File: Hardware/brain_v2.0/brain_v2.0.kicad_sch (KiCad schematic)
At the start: 84 parts, among them J1 Conn_01x02, J10 RFID, J11 Conn_01x05, J12 Conn_01x02, J13 Conn_01x02, J14 Conn_01x02, J15 Conn_01x04, J16 Conn_01x04, J2 Conn_01x02, J3 Conn_01x03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

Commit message: second version of brain
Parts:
- added TP7: TestPoint, TestPoint:TestPoint_Keystone_5010-5014_Multipurpose, symbol Connector:TestPoint
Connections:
- net GPIO0: now also TP7.1

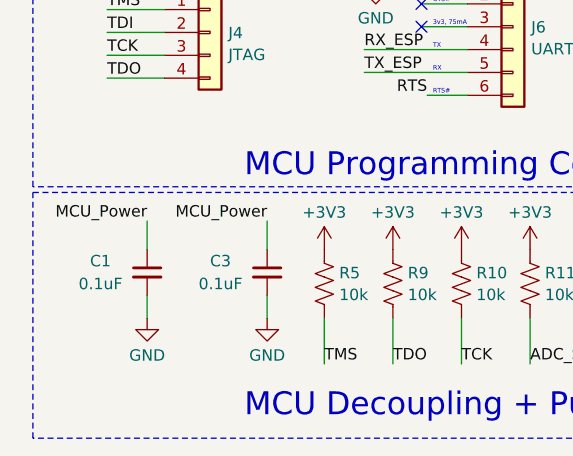
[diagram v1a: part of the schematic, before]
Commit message: creating PDS board and update other boards
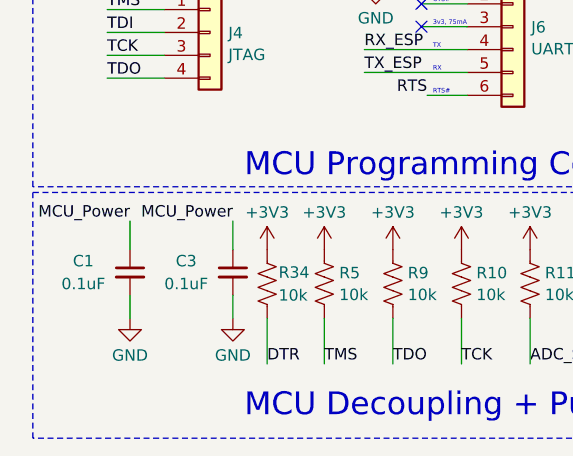
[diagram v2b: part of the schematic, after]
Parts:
- added R34: 10k, Resistor_SMD:R_1206_3216Metric, symbol Device:R_US
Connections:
- net +3V3: now also R34.1
- net DTR: now also R34.2
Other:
- moved on the sheet: C1, C3
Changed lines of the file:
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@@
     (stroke (width 0) (type default))
   )
-  (wire (pts (xy 24.765 190.5) (xy 24.765 187.96))
+  (wire (pts (xy 22.86 190.5) (xy 22.86 187.96))
     (stroke (width 0) (type default))
   )
@@
     (stroke (width 0) (type default))
   )
-  (wire (pts (xy 38.1 190.5) (xy 38.1 187.96))
+  (wire (pts (xy 34.29 190.5) (xy 34.29 187.96))
     (stroke (width 0) (type default))
   )
@@
     (stroke (width 0) (type default))
   )
-  (wire (pts (xy 38.1 179.705) (xy 38.1 182.88))
+  (wire (pts (xy 34.29 179.705) (xy 34.29 182.88))
     (stroke (width 0) (type default))
   )
@@
     (stroke (width 0) (type default))
   )
+  (wire (pts (xy 38.1 190.5) (xy 38.1 195.58))
+    (stroke (width 0) (type default))
+  )
   (wire (pts (xy 175.26 133.35) (xy 177.8 133.35))
     (stroke (width 0) (type default))
@@
     (stroke (width 0) (type default))
   )
-  (wire (pts (xy 24.765 179.705) (xy 24.765 182.88))
+  (wire (pts (xy 22.86 179.705) (xy 22.86 182.88))
     (stroke (width 0) (type default))
   )
@@
     (effects (font (size 1.27 1.27)) (justify left bottom))
   )
-  (label "MCU_Power" (at 38.1 179.705 180) (fields_autoplaced)
+  (label "MCU_Power" (at 34.29 179.705 180) (fields_autoplaced)
     (effects (font (size 1.27 1.27)) (justify right bottom))
   )
@@
     (effects (font (size 1.27 1.27)) (justify left bottom))
   )
+  (label "DTR" (at 38.1 195.58 0) (fields_autoplaced)
+    (effects (font (size 1.27 1.27)) (justify left bottom))
+  )
   (label "ADC_SDA" (at 246.38 148.59 0) (fields_autoplaced)
     (effects (font (size 1.27 1.27)) (justify left bottom))
@@
     (effects (font (size 1.27 1.27)) (justify left bottom))
   )
-  (label "MCU_Power" (at 24.765 179.705 180) (fields_autoplaced)
+  (label "MCU_Power" (at 22.86 179.705 180) (fields_autoplaced)
     (effects (font (size 1.27 1.27)) (justify right bottom))
   )
@@
     )
   )
-  (symbol (lib_id "device:C_Small") (at 24.765 185.42 0) (unit 1)
+  (symbol (lib_id "device:C_Small") (at 22.86 185.42 0) (unit 1)
     (in_bom yes) (on_board yes) (dnp no)
-    (property "Reference" "C1" (at 18.415 184.15 0)
+    (property "Reference" "C1" (at 16.51 184.15 0)
       (effects (font (size 1.27 1.27)) (justify left))
     )
-    (property "Value" "0.1uF" (at 17.145 186.69 0)
+    (property "Value" "0.1uF" (at 15.24 186.69 0)
       (effects (font (size 1.27 1.27)) (justify left))
     )
-    (property "Footprint" "Capacitor_SMD:C_0603_1608Metric" (at 24.765 185.42 0)
+    (property "Footprint" "Capacitor_SMD:C_0603_1608Metric" (at 22.86 185.42 0)
       (effects (font (size 1.27 1.27)) hide)
     )
-    (property "Datasheet" "~" (at 24.765 185.42 0)
+    (property "Datasheet" "~" (at 22.86 185.42 0)
       (effects (font (size 1.27 1.27)) hide)
     )
-    (property "Link" "https://www.digikey.com/en/products/detail/kemet/C0603C103F3GECAUTO/6826352" (at 24.765 185.42 0)
+    (property "Link" "https://www.digikey.com/en/products/detail/kemet/C0603C103F3GECAUTO/6826352" (at 22.86 185.42 0)
       (effects (font (size 1.27 1.27)) hide)
     )
-    (property "MPN" "C0603C103F3GECAUTO" (at 24.765 185.42 0)
+    (property "MPN" "C0603C103F3GECAUTO" (at 22.86 185.42 0)
       (effects (font (size 1.27 1.27)) hide)
     )
@@
     )
   )
-  (symbol (lib_id "power:GND") (at 24.765 190.5 0) (unit 1)
+  (symbol (lib_id "power:GND") (at 22.86 190.5 0) (unit 1)
     (in_bom yes) (on_board yes) (dnp no) (fields_autoplaced)
-    (property "Reference" "#PWR03" (at 24.765 196.85 0)
+    (property "Reference" "#PWR03" (at 22.86 196.85 0)
       (effects (font (size 1.27 1.27)) hide)
     )
-    (property "Value" "GND" (at 24.765 194.6331 0)
+    (property "Value" "GND" (at 22.86 194.6331 0)
       (effects (font (size 1.27 1.27)))
     )
-    (property "Footprint" "" (at 24.765 190.5 0)
+    (property "Footprint" "" (at 22.86 190.5 0)
       (effects (font (size 1.27 1.27)) hide)
     )
-    (property "Datasheet" "" (at 24.765 190.5 0)
+    (property "Datasheet" "" (at 22.86 190.5 0)
       (effects (font (size 1.27 1.27)) hide)
     )
@@
     )
   )
+  (symbol (lib_id "power:+3V3") (at 38.1 182.88 0) (unit 1)
+    (in_bom yes) (on_board yes) (dnp no) (fields_autoplaced)
+    (property "Reference" "#PWR059" (at 38.1 186.69 0)
+      (effects (font (size 1.27 1.27)) hide)
+    )
+    (property "Value" "+3V3" (at 38.1 178.7469 0)
+      (effects (font (size 1.27 1.27)))
+    )
+    (property "Footprint" "" (at 38.1 182.88 0)
+      (effects (font (size 1.27 1.27)) hide)
+    )
+    (property "Datasheet" "" (at 38.1 182.88 0)
+      (effects (font (size 1.27 1.27)) hide)
+    )
+    (pin "1")
+    (instances
+      (project "brain_v2.0"
+        (path "/1e1b062d-fad0-427c-a622-c5b8a80b5268"
+          (reference "#PWR059") (unit 1)
+        )
+      )
+    )
+  )
   (symbol (lib_id "Mechanical:MountingHole") (at 17.145 15.875 0) (unit 1)
     (in_bom yes) (on_board yes) (dnp no) (fields_autoplaced)
@@
     )
   )
-  (symbol (lib_id "power:GND") (at 38.1 190.5 0) (unit 1)
+  (symbol (lib_id "power:GND") (at 34.29 190.5 0) (unit 1)
     (in_bom yes) (on_board yes) (dnp no) (fields_autoplaced)
-    (property "Reference" "#PWR010" (at 38.1 196.85 0)
+    (property "Reference" "#PWR010" (at 34.29 196.85 0)
       (effects (font (size 1.27 1.27)) hide)
     )
-    (property "Value" "GND" (at 38.1 194.6331 0)
+    (property "Value" "GND" (at 34.29 194.6331 0)
       (effects (font (size 1.27 1.27)))
     )
-    (property "Footprint" "" (at 38.1 190.5 0)
+    (property "Footprint" "" (at 34.29 190.5 0)
       (effects (font (size 1.27 1.27)) hide)
     )
-    (property "Datasheet" "" (at 38.1 190.5 0)
+    (property "Datasheet" "" (at 34.29 190.5 0)
       (effects (font (size 1.27 1.27)) hide)
     )
@@
     )
   )
+  (symbol (lib_id "Device:R_US") (at 38.1 186.69 0) (unit 1)
+    (in_bom yes) (on_board yes) (dnp no)
+    (property "Reference" "R34" (at 39.37 185.42 0)
+      (effects (font (size 1.27 1.27)) (justify left))
+    )
+    (property "Value" "10k" (at 39.37 187.96 0)
+      (effects (font (size 1.27 1.27)) (justify left))
+    )
+    (property "Footprint" "Resistor_SMD:R_1206_3216Metric" (at 39.116 186.944 90)
+      (effects (font (size 1.27 1.27)) hide)
+    )
+    (property "Datasheet" "~" (at 38.1 186.69 0)
+      (effects (font (size 1.27 1.27)) hide)
+    )
+    (property "Link" "https://www.digikey.com/en/products/detail/susumu/HRG3216P-1002-B-T1/5762469" (at 38.1 186.69 0)
+      (effects (font (size 1.27 1.27)) hide)
+    )
+    (property "MPN" "HRG3216P-1002-B-T1" (at 38.1 186.69 0)
+      (effects (font (size 1.27 1.27)) hide)
+    )
+    (pin "1")
+    (pin "2")
+    (instances
+      (project "brain_v2.0"
+        (path "/1e1b062d-fad0-427c-a622-c5b8a80b5268"
+          (reference "R34") (unit 1)
+        )
+      )
+    )
+  )
   (symbol (lib_id "Connector_Generic:Conn_01x02") (at 19.685 56.515 180) (unit 1)
     (in_bom yes) (on_board yes) (dnp no) (fields_autoplaced)
@@
     )
   )
-  (symbol (lib_id "device:C_Small") (at 38.1 185.42 0) (unit 1)
+  (symbol (lib_id "device:C_Small") (at 34.29 185.42 0) (unit 1)
     (in_bom yes) (on_board yes) (dnp no)
-    (property "Reference" "C3" (at 31.75 184.15 0)
+    (property "Reference" "C3" (at 27.94 184.15 0)
       (effects (font (size 1.27 1.27)) (justify left))
     )
-    (property "Value" "0.1uF" (at 30.48 186.69 0)
+    (property "Value" "0.1uF" (at 26.67 186.69 0)
       (effects (font (size 1.27 1.27)) (justify left))
     )
-    (property "Footprint" "Capacitor_SMD:C_0603_1608Metric" (at 38.1 185.42 0)
+    (property "Footprint" "Capacitor_SMD:C_0603_1608Metric" (at 34.29 185.42 0)
       (effects (font (size 1.27 1.27)) hide)
     )
-    (property "Datasheet" "~" (at 38.1 185.42 0)
+    (property "Datasheet" "~" (at 34.29 185.42 0)
       (effects (font (size 1.27 1.27)) hide)
     )
-    (property "Link" "https://www.digikey.com/en/products/detail/kemet/C0603C103F3GECAUTO/6826352" (at 38.1 185.42 0)
+    (property "Link" "https://www.digikey.com/en/products/detail/kemet/C0603C103F3GECAUTO/6826352" (at 34.29 185.42 0)
       (effects (font (size 1.27 1.27)) hide)
     )
-    (property "MPN" "C0603C103F3GECAUTO" (at 38.1 185.42 0)
+    (property "MPN" "C0603C103F3GECAUTO" (at 34.29 185.42 0)
       (effects (font (size 1.27 1.27)) hide)
     )
